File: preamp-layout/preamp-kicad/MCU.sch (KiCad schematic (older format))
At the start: 10 parts, among them J20 Conn_01x15_Female, J21 Conn_01x15_Female, J22 Conn_01x06_Female, J23 Conn_01x03_Female, J24 Conn_01x03_Female, J25 Conn_01x03_Female, J26 Conn_01x03_Male, J27 Conn_01x02_Male, J28 Conn_01x02_Male, U5 ESP32-DevKitC

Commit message: BOM Update
parts added to BOM, connector cleanup. Stopping point before renumbering refdes in a more intelligent way.
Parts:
- renumbered J20 to J27, J21 to J28, J22 to J29, J23 to J30, J24 to J31, J25 to J32, J26 to J33, J27 to J34, J28 to J35
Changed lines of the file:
@@
 $Descr A4 11693 8268
 encoding utf-8
-Sheet 7 13
+Sheet 6 13
 Title "Preamp MCU Board"
 Date "2020-02-25"
@@
 PWR, monitoring
 $Comp
-L Connector:Conn_01x02_Male J28
+L Connector:Conn_01x02_Male J35
 U 1 1 63AD6EFD
 P 8600 3750
-F 0 "J28" H 8572 3678 50  0000 R CNN
+F 0 "J35" H 8572 3678 50  0000 R CNN
 F 1 "Conn_01x02_Male" H 8572 3633 50  0001 R CNN
 F 2 "Connector_JST:JST_EH_B2B-EH-A_1x02_P2.50mm_Vertical" H 8600 3750 50  0001 C CNN
@@
 AR Path="/5E607732/6496C10E" Ref="J?"  Part="1"
 AR Path="/5E2D8DA2/6496C10E" Ref="J?"  Part="1"
-AR Path="/619FA14B/6496C10E" Ref="J23"  Part="1"
-F 0 "J23" H 7278 4180 50  0000 L CNN
+AR Path="/619FA14B/6496C10E" Ref="J30"  Part="1"
+F 0 "J30" H 7278 4180 50  0000 L CNN
 F 1 "Conn_01x03_Female" H 7278 4135 50  0001 L CNN
 F 2 "Connector_PinHeader_2.54mm:PinHeader_1x03_P2.54mm_Vertical" H 7250 4200 50  0001 C CNN
@@
 P 8350 4900
 AR Path="/5E2D8DA2/6496C114" Ref="J?"  Part="1"
-AR Path="/619FA14B/6496C114" Ref="J26"  Part="1"
-F 0 "J26" H 8322 4878 50  0000 R CNN
+AR Path="/619FA14B/6496C114" Ref="J33"  Part="1"
+F 0 "J33" H 8322 4878 50  0000 R CNN
 F 1 "Conn_01x03_Male" H 8322 4833 50  0001 R CNN
 F 2 "Connector_PinHeader_2.54mm:PinHeader_1x03_P2.54mm_Vertical" H 8350 4900 50  0001 C CNN
@@
 AR Path="/5E607732/6496FD14" Ref="J?"  Part="1"
 AR Path="/5E2D8DA2/6496FD14" Ref="J?"  Part="1"
-AR Path="/619FA14B/6496FD14" Ref="J24"  Part="1"
-F 0 "J24" H 7278 4630 50  0000 L CNN
+AR Path="/619FA14B/6496FD14" Ref="J31"  Part="1"
+F 0 "J31" H 7278 4630 50  0000 L CNN
 F 1 "Conn_01x03_Female" H 7278 4585 50  0001 L CNN
 F 2 "Connector_PinHeader_2.54mm:PinHeader_1x03_P2.54mm_Vertical" H 7250 4650 50  0001 C CNN
@@
 AR Path="/5E607732/64973E6E" Ref="J?"  Part="1"
 AR Path="/5E2D8DA2/64973E6E" Ref="J?"  Part="1"
-AR Path="/619FA14B/64973E6E" Ref="J25"  Part="1"
-F 0 "J25" H 7278 5080 50  0000 L CNN
+AR Path="/619FA14B/64973E6E" Ref="J32"  Part="1"
+F 0 "J32" H 7278 5080 50  0000 L CNN
 F 1 "Conn_01x03_Female" H 7278 5035 50  0001 L CNN
 F 2 "Connector_PinHeader_2.54mm:PinHeader_1x03_P2.54mm_Vertical" H 7250 5100 50  0001 C CNN
@@
 MISO
 $Comp
-L Connector:Conn_01x06_Female J22
+L Connector:Conn_01x06_Female J29
 U 1 1 64977856
 P 7250 3350
-F 0 "J22" H 7278 3280 50  0000 L CNN
+F 0 "J29" H 7278 3280 50  0000 L CNN
 F 1 "Conn_01x06_Female" H 7278 3235 50  0001 L CNN
 F 2 "Connector_PinHeader_2.54mm:PinHeader_1x06_P2.54mm_Vertical" H 7250 3350 50  0001 C CNN
@@
 CS_IO
 $Comp
-L Connector:Conn_01x15_Female J21
+L Connector:Conn_01x15_Female J28
 U 1 1 649C22F5
 P 5200 3850
-F 0 "J21" H 5092 4643 50  0000 C CNN
+F 0 "J28" H 5092 4643 50  0000 C CNN
 F 1 "Conn_01x15_Female" H 5092 4644 50  0001 C CNN
 F 2 "Connector_PinHeader_2.54mm:PinHeader_1x15_P2.54mm_Vertical" H 5200 3850 50  0001 C CNN
@@
 $EndComp
 $Comp
-L Connector:Conn_01x15_Female J20
+L Connector:Conn_01x15_Female J27
 U 1 1 649C438C
 P 3800 3850
-F 0 "J20" H 3828 3830 50  0000 L CNN
+F 0 "J27" H 3828 3830 50  0000 L CNN
 F 1 "Conn_01x15_Female" H 3828 3785 50  0001 L CNN
 F 2 "Connector_PinHeader_2.54mm:PinHeader_1x15_P2.54mm_Vertical" H 3800 3850 50  0001 C CNN
@@
 P 3350 4750
 AR Path="/5E26F6FE/64EF3AEF" Ref="#PWR?"  Part="1"
-AR Path="/619FA14B/64EF3AEF" Ref="#PWR024"  Part="1"
-F 0 "#PWR024" H 3350 4500 50  0001 C CNN
+AR Path="/619FA14B/64EF3AEF" Ref="#PWR031"  Part="1"
+F 0 "#PWR031" H 3350 4500 50  0001 C CNN
 F 1 "GND" H 3355 4577 50  0000 C CNN
 F 2 "" H 3350 4750 50  0001 C CNN
@@
 P 8400 3400
 AR Path="/5E26F6FE/64EF440C" Ref="#PWR?"  Part="1"
-AR Path="/619FA14B/64EF440C" Ref="#PWR025"  Part="1"
-F 0 "#PWR025" H 8400 3150 50  0001 C CNN
+AR Path="/619FA14B/64EF440C" Ref="#PWR033"  Part="1"
+F 0 "#PWR033" H 8400 3150 50  0001 C CNN
 F 1 "GND" H 8405 3227 50  0000 C CNN
 F 2 "" H 8400 3400 50  0001 C CNN
@@
 P 8400 3950
 AR Path="/5E26F6FE/64EF4C33" Ref="#PWR?"  Part="1"
-AR Path="/619FA14B/64EF4C33" Ref="#PWR026"  Part="1"
-F 0 "#PWR026" H 8400 3700 50  0001 C CNN
+AR Path="/619FA14B/64EF4C33" Ref="#PWR034"  Part="1"
+F 0 "#PWR034" H 8400 3700 50  0001 C CNN
 F 1 "GND" H 8405 3777 50  0000 C CNN
 F 2 "" H 8400 3950 50  0001 C CNN
@@
 NoConn ~ 7050 3650
 $Comp
-L Connector:Conn_01x02_Male J27
+L Connector:Conn_01x02_Male J34
 U 1 1 5E6537E3
 P 8600 3200
-F 0 "J27" H 8572 3128 50  0000 R CNN
+F 0 "J34" H 8572 3128 50  0000 R CNN
 F 1 "Conn_01x02_Male" H 8572 3083 50  0001 R CNN
 F 2 "Connector_JST:JST_EH_B2B-EH-A_1x02_P2.50mm_Vertical" H 8600 3200 50  0001 C CNN
@@
 P 8050 5100
 AR Path="/5E26F6FE/5EA8A311" Ref="#PWR?"  Part="1"
-AR Path="/619FA14B/5EA8A311" Ref="#PWR021"  Part="1"
-F 0 "#PWR021" H 8050 4850 50  0001 C CNN
+AR Path="/619FA14B/5EA8A311" Ref="#PWR032"  Part="1"
+F 0 "#PWR032" H 8050 4850 50  0001 C CNN
 F 1 "GND" H 8055 4927 50  0000 C CNN
 F 2 "" H 8050 5100 50  0001 C CNN

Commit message: Schematic Updates
Updated pin connections for DAC, footprint updates, MCU connections.
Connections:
- wire segments 21 -> 5
- no-connect marks 51 -> 46
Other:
- moved on the sheet: J33, J35
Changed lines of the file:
@@
 Comment4 "Author: Jordon Gerber"
 $EndDescr
-Text HLabel 3550 2200 0    50   Input ~ 0
+Text HLabel 5400 3250 2    50   Input ~ 0
 MISO
-Text HLabel 5700 3150 2    50   Output ~ 0
+Text HLabel 5400 3150 2    50   Output ~ 0
 MOSI
-Text HLabel 5700 3750 2    50   Output ~ 0
+Text HLabel 5400 3750 2    50   Output ~ 0
 CLK
-Text HLabel 5700 3850 2    50   Output ~ 0
+Text HLabel 5400 3850 2    50   Output ~ 0
 CS_IO
 Wire Wire Line
-	8400 3850 8400 3950
-Wire Wire Line
-	8300 3750 8400 3750
-Text GLabel 8300 3750 0    50   UnSpc ~ 0
+	8400 3950 8400 4050
+Text GLabel 8400 3850 0    50   UnSpc ~ 0
 +5V
 Wire Wire Line
 	8400 3300 8400 3400
-Wire Wire Line
-	8300 3200 8400 3200
-Text GLabel 8300 3200 0    50   UnSpc ~ 0
+Text GLabel 8400 3200 0    50   UnSpc ~ 0
 +5V
 Text Notes 8150 2750 0    50   ~ 0
@@
 L Connector:Conn_01x02_Male J35
 U 1 1 63AD6EFD
-P 8600 3750
-F 0 "J35" H 8572 3678 50  0000 R CNN
-F 1 "Conn_01x02_Male" H 8572 3633 50  0001 R CNN
-F 2 "Connector_JST:JST_EH_B2B-EH-A_1x02_P2.50mm_Vertical" H 8600 3750 50  0001 C CNN
-F 3 "~" H 8600 3750 50  0001 C CNN
-	1    8600 3750
-	-1   0    0    -1
-$EndComp
-Text HLabel 3300 3750 0    50   Input ~ 0
+P 8600 3850
+F 0 "J35" H 8572 3778 50  0000 R CNN
+F 1 "Conn_01x02_Male" H 8572 3733 50  0001 R CNN
+F 2 "Connector_JST:JST_EH_B2B-EH-A_1x02_P2.50mm_Vertical" H 8600 3850 50  0001 C CNN
+F 3 "~" H 8600 3850 50  0001 C CNN
+	1    8600 3850
+	-1   0    0    -1
+$EndComp
+Text HLabel 3600 3750 0    50   Input ~ 0
 SEL_CLK
-Text HLabel 3300 3950 0    50   Input ~ 0
+Text HLabel 3600 3950 0    50   Input ~ 0
 SEL_SW
-Text HLabel 3300 4050 0    50   Input ~ 0
+Text HLabel 3600 4050 0    50   Input ~ 0
 VOL_CLK
-Text HLabel 3300 4150 0    50   Input ~ 0
+Text HLabel 3600 4150 0    50   Input ~ 0
 VOL_DT
-Text HLabel 3300 4350 0    50   Input ~ 0
+Text HLabel 3600 4350 0    50   Input ~ 0
 VOL_SW
-Text HLabel 3550 2400 0    50   Output ~ 0
+Text HLabel 5400 4150 2    50   Output ~ 0
 CS_FP
-Text HLabel 3550 2500 0    50   Output ~ 0
+Text HLabel 5400 4050 2    50   Output ~ 0
 CS_VOL_HP
 Text HLabel 8050 4900 0    50   Output ~ 0
 LED_DT
-Text HLabel 3550 2600 0    50   Output ~ 0
+Text HLabel 5400 3950 2    50   Output ~ 0
 CS_VOL_MAIN
-Text GLabel 3550 4700 3    50   UnSpc ~ 0
+Text GLabel 3600 4550 0    50   UnSpc ~ 0
 +5V
 Wire Wire Line
@@
 	1    0    0    -1
 $EndComp
-Text HLabel 3300 3850 0    50   Input ~ 0
+Text HLabel 3600 3850 0    50   Input ~ 0
 SEL_DT
 Wire Wire Line
-	3550 4550 3600 4550
-Wire Wire Line
-	3550 4550 3550 4700
-Wire Wire Line
 	3350 4450 3600 4450
-Wire Wire Line
-	3300 3750 3600 3750
-Wire Wire Line
-	3300 3850 3600 3850
-Wire Wire Line
-	3300 3950 3600 3950
-Wire Wire Line
-	3300 4050 3600 4050
-Wire Wire Line
-	3300 4150 3600 4150
-Wire Wire Line
-	3300 4350 3600 4350
-Wire Wire Line
-	5400 3150 5700 3150
-Wire Wire Line
-	5400 3750 5700 3750
-Wire Wire Line
-	5400 3850 5700 3850
 $Comp
 L Connector:Conn_01x03_Female J?
@@
 L Connector:Conn_01x03_Male J?
 U 1 1 6496C114
-P 8350 4900
+P 8250 4900
 AR Path="/5E2D8DA2/6496C114" Ref="J?"  Part="1"
 AR Path="/619FA14B/6496C114" Ref="J33"  Part="1"
-F 0 "J33" H 8322 4878 50  0000 R CNN
-F 1 "Conn_01x03_Male" H 8322 4833 50  0001 R CNN
-F 2 "Connector_PinHeader_2.54mm:PinHeader_1x03_P2.54mm_Vertical" H 8350 4900 50  0001 C CNN
-F 3 "~" H 8350 4900 50  0001 C CNN
-	1    8350 4900
+F 0 "J33" H 8222 4878 50  0000 R CNN
+F 1 "Conn_01x03_Male" H 8222 4833 50  0001 R CNN
+F 2 "Connector_PinHeader_2.54mm:PinHeader_1x03_P2.54mm_Vertical" H 8250 4900 50  0001 C CNN
+F 3 "~" H 8250 4900 50  0001 C CNN
+	1    8250 4900
 	-1   0    0    -1
 $EndComp
@@
 L power:GND #PWR?
 U 1 1 64EF4C33
-P 8400 3950
+P 8400 4050
 AR Path="/5E26F6FE/64EF4C33" Ref="#PWR?"  Part="1"
 AR Path="/619FA14B/64EF4C33" Ref="#PWR034"  Part="1"
-F 0 "#PWR034" H 8400 3700 50  0001 C CNN
-F 1 "GND" H 8405 3777 50  0000 C CNN
-F 2 "" H 8400 3950 50  0001 C CNN
-F 3 "" H 8400 3950 50  0001 C CNN
-	1    8400 3950
+F 0 "#PWR034" H 8400 3800 50  0001 C CNN
+F 1 "GND" H 8405 3877 50  0000 C CNN
+F 2 "" H 8400 4050 50  0001 C CNN
+F 3 "" H 8400 4050 50  0001 C CNN
+	1    8400 4050
 	1    0    0    -1
 $EndComp
@@
 NoConn ~ 4950 3350
 NoConn ~ 4950 3450
-NoConn ~ 5400 3250
 NoConn ~ 5400 3350
 NoConn ~ 5400 3450
 NoConn ~ 5400 3550
 NoConn ~ 5400 3650
-NoConn ~ 5400 3950
-NoConn ~ 5400 4050
-NoConn ~ 5400 4150
 NoConn ~ 5400 4250
 NoConn ~ 5400 4350
@@
 NoConn ~ 3600 3250
 NoConn ~ 3600 3350
-NoConn ~ 3600 3450
 NoConn ~ 3600 3550
 NoConn ~ 3600 3650
@@
 Text GLabel 8050 4800 0    50   UnSpc ~ 0
 +5V
-Wire Wire Line
-	8050 4800 8150 4800
-Wire Wire Line
-	8050 4900 8150 4900
-Wire Wire Line
-	8050 5000 8150 5000
+Text HLabel 3600 3450 0    50   Output ~ 0
+LED_DT
 $EndSCHEMATC

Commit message: Footprint updates
Footprint creation of relay, ESP32
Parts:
- removed J27, J28: Conn_01x15_Female, Connector_PinHeader_2.54mm:PinHeader_1x15_P2.54mm_Vertical, symbol Connector:Conn_01x15_Female
- U5: footprint (none) -> preamp:ESP32_MELIFE_DEVKIT
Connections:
- wire segments 5 -> 34
- no-connect marks 46 -> 16
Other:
- moved on the sheet: U5
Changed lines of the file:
@@
 Comment4 "Author: Jordon Gerber"
 $EndDescr
-Text HLabel 5400 3250 2    50   Input ~ 0
-MISO
-Text HLabel 5400 3150 2    50   Output ~ 0
-MOSI
-Text HLabel 5400 3750 2    50   Output ~ 0
-CLK
-Text HLabel 5400 3850 2    50   Output ~ 0
-CS_IO
 Wire Wire Line
 	8400 3950 8400 4050
@@
 	-1   0    0    -1
 $EndComp
-Text HLabel 3600 3750 0    50   Input ~ 0
+Text HLabel 4000 3550 0    50   Input ~ 0
 SEL_CLK
-Text HLabel 3600 3950 0    50   Input ~ 0
+Text HLabel 4000 3750 0    50   Input ~ 0
 SEL_SW
-Text HLabel 3600 4050 0    50   Input ~ 0
+Text HLabel 4000 3850 0    50   Input ~ 0
 VOL_CLK
-Text HLabel 3600 4150 0    50   Input ~ 0
+Text HLabel 4000 3950 0    50   Input ~ 0
 VOL_DT
-Text HLabel 3600 4350 0    50   Input ~ 0
+Text HLabel 4000 4150 0    50   Input ~ 0
 VOL_SW
-Text HLabel 5400 4150 2    50   Output ~ 0
-CS_FP
-Text HLabel 5400 4050 2    50   Output ~ 0
-CS_VOL_HP
 Text HLabel 8050 4900 0    50   Output ~ 0
 LED_DT
-Text HLabel 5400 3950 2    50   Output ~ 0
-CS_VOL_MAIN
-Text GLabel 3600 4550 0    50   UnSpc ~ 0
+Text GLabel 4000 4350 0    50   UnSpc ~ 0
 +5V
 Wire Wire Line
-	3350 4750 3350 4450
+	3750 4550 3750 4250
 $Comp
 L preamp:ESP32-DevKitC U5
 U 1 1 64954378
-P 4500 3850
-F 0 "U5" H 4500 4815 50  0000 C CNN
-F 1 "ESP32-DevKitC" H 4500 4724 50  0000 C CNN
-F 2 "" H 4500 4850 50  0001 C CNN
-F 3 "" H 4500 4850 50  0001 C CNN
-	1    4500 3850
-	1    0    0    -1
-$EndComp
-Text HLabel 3600 3850 0    50   Input ~ 0
+P 4550 3650
+F 0 "U5" H 4550 4615 50  0000 C CNN
+F 1 "ESP32-DevKitC" H 4550 4524 50  0000 C CNN
+F 2 "preamp:ESP32_MELIFE_DEVKIT" H 4550 4650 50  0001 C CNN
+F 3 "" H 4550 4650 50  0001 C CNN
+	1    4550 3650
+	1    0    0    -1
+$EndComp
+Text HLabel 4000 3650 0    50   Input ~ 0
 SEL_DT
-Wire Wire Line
-	3350 4450 3600 4450
 $Comp
 L Connector:Conn_01x03_Female J?
@@
 CS_IO
 $Comp
-L Connector:Conn_01x15_Female J28
-U 1 1 649C22F5
-P 5200 3850
-F 0 "J28" H 5092 4643 50  0000 C CNN
-F 1 "Conn_01x15_Female" H 5092 4644 50  0001 C CNN
-F 2 "Connector_PinHeader_2.54mm:PinHeader_1x15_P2.54mm_Vertical" H 5200 3850 50  0001 C CNN
-F 3 "~" H 5200 3850 50  0001 C CNN
-	1    5200 3850
-	-1   0    0    -1
-$EndComp
-$Comp
-L Connector:Conn_01x15_Female J27
-U 1 1 649C438C
-P 3800 3850
-F 0 "J27" H 3828 3830 50  0000 L CNN
-F 1 "Conn_01x15_Female" H 3828 3785 50  0001 L CNN
-F 2 "Connector_PinHeader_2.54mm:PinHeader_1x15_P2.54mm_Vertical" H 3800 3850 50  0001 C CNN
-F 3 "~" H 3800 3850 50  0001 C CNN
-	1    3800 3850
-	1    0    0    -1
-$EndComp
-$Comp
 L power:GND #PWR?
 U 1 1 64EF3AEF
-P 3350 4750
+P 3750 4550
 AR Path="/5E26F6FE/64EF3AEF" Ref="#PWR?"  Part="1"
 AR Path="/619FA14B/64EF3AEF" Ref="#PWR031"  Part="1"
-F 0 "#PWR031" H 3350 4500 50  0001 C CNN
-F 1 "GND" H 3355 4577 50  0000 C CNN
-F 2 "" H 3350 4750 50  0001 C CNN
-F 3 "" H 3350 4750 50  0001 C CNN
-	1    3350 4750
+F 0 "#PWR031" H 3750 4300 50  0001 C CNN
+F 1 "GND" H 3755 4377 50  0000 C CNN
+F 2 "" H 3750 4550 50  0001 C CNN
+F 3 "" H 3750 4550 50  0001 C CNN
+	1    3750 4550
 	1    0    0    -1
 $EndComp
@@
 	1    0    0    -1
 $EndComp
-NoConn ~ 4950 4550
-NoConn ~ 4950 4450
-NoConn ~ 4950 4350
-NoConn ~ 4950 4250
-NoConn ~ 4950 4150
-NoConn ~ 4950 4050
-NoConn ~ 4950 3950
-NoConn ~ 4950 3850
-NoConn ~ 4950 3750
-NoConn ~ 4950 3650
-NoConn ~ 4950 3550
-NoConn ~ 4950 3150
-NoConn ~ 4950 3250
-NoConn ~ 4950 3350
-NoConn ~ 4950 3450
-NoConn ~ 5400 3350
-NoConn ~ 5400 3450
-NoConn ~ 5400 3550
-NoConn ~ 5400 3650
-NoConn ~ 5400 4250
-NoConn ~ 5400 4350
-NoConn ~ 5400 4450
-NoConn ~ 5400 4550
-NoConn ~ 4050 4550
-NoConn ~ 4050 4450
-NoConn ~ 4050 4350
-NoConn ~ 4050 4250
-NoConn ~ 4050 4150
-NoConn ~ 4050 4050
-NoConn ~ 4050 3950
-NoConn ~ 4050 3850
-NoConn ~ 4050 3750
-NoConn ~ 4050 3650
-NoConn ~ 4050 3550
-NoConn ~ 4050 3450
-NoConn ~ 4050 3350
-NoConn ~ 4050 3250
-NoConn ~ 4050 3150
-NoConn ~ 3600 3150
-NoConn ~ 3600 3250
-NoConn ~ 3600 3350
-NoConn ~ 3600 3550
-NoConn ~ 3600 3650
-NoConn ~ 3600 4250
+NoConn ~ 4000 2950
+NoConn ~ 4000 3050
+NoConn ~ 4000 3150
+NoConn ~ 4000 3350
+NoConn ~ 4000 3450
+NoConn ~ 4000 4050
 NoConn ~ 7050 3550
 NoConn ~ 7050 3650
@@
 Text GLabel 8050 4800 0    50   UnSpc ~ 0
 +5V
-Text HLabel 3600 3450 0    50   Output ~ 0
+Text HLabel 4000 3250 0    50   Output ~ 0
 LED_DT
+NoConn ~ 5100 4350
+NoConn ~ 5100 4250
+NoConn ~ 5100 4150
+NoConn ~ 5100 4050
+NoConn ~ 5100 3450
+NoConn ~ 5100 3350
+NoConn ~ 5100 3250
+NoConn ~ 5100 3150
+Text HLabel 5100 3750 2    50   Output ~ 0
+CS_VOL_MAIN
+Text HLabel 5100 3850 2    50   Output ~ 0
+CS_VOL_HP
+Text HLabel 5100 3950 2    50   Output ~ 0
+CS_FP
+Text HLabel 5100 3650 2    50   Output ~ 0
+CS_IO
+Text HLabel 5100 3550 2    50   Output ~ 0
+CLK
+Text HLabel 5100 2950 2    50   Output ~ 0
+MOSI
+Text HLabel 5100 3050 2    50   Input ~ 0
+MISO
+Wire Wire Line
+	5000 3050 5100 3050
+Wire Wire Line
+	5000 2950 5100 2950
+Wire Wire Line
+	5000 3250 5100 3250
+Wire Wire Line
+	5000 3150 5100 3150
+Wire Wire Line
+	5000 3450 5100 3450
+Wire Wire Line
+	5000 3350 5100 3350
+Wire Wire Line
+	5000 3650 5100 3650
+Wire Wire Line
+	5000 3550 5100 3550
+Wire Wire Line
+	5000 3850 5100 3850
+Wire Wire Line
+	5000 3750 5100 3750
+Wire Wire Line
+	5000 4050 5100 4050
+Wire Wire Line
+	5000 3950 5100 3950
+Wire Wire Line
+	5000 4250 5100 4250
+Wire Wire Line
+	5000 4150 5100 4150
+Wire Wire Line
+	5000 4350 5100 4350
+Wire Wire Line
+	4000 3050 4100 3050
+Wire Wire Line
+	4000 2950 4100 2950
+Wire Wire Line
+	4000 3250 4100 3250
+Wire Wire Line
+	4000 3150 4100 3150
+Wire Wire Line
+	4000 3450 4100 3450
+Wire Wire Line
+	4000 3350 4100 3350
+Wire Wire Line
+	4000 3650 4100 3650
+Wire Wire Line
+	4000 3550 4100 3550
+Wire Wire Line
+	4000 3850 4100 3850
+Wire Wire Line
+	4000 3750 4100 3750
+Wire Wire Line
+	4000 4050 4100 4050
+Wire Wire Line
+	4000 3950 4100 3950
+Wire Wire Line
+	4000 4150 4100 4150
+Wire Wire Line
+	4000 4350 4100 4350
+Wire Wire Line
+	3750 4250 4100 4250
 $EndSCHEMATC

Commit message: Conn / Pin Updates
Updated cable headers, pin names, MCU conn layout. MCP4902 changeout for custom symbol.
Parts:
- removed J29: Conn_01x06_Female, Connector_PinHeader_2.54mm:PinHeader_1x06_P2.54mm_Vertical, symbol Connector:Conn_01x06_Female
- removed J30, J31, J32: Conn_01x03_Female, Connector_PinHeader_2.54mm:PinHeader_1x03_P2.54mm_Vertical, symbol Connector:Conn_01x03_Female
- added J27, J32: Conn_01x04_Female, symbol Connector:Conn_01x04_Female
- added J29, J30, J31: Conn_01x05_Female, symbol Connector:Conn_01x05_Female
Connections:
- net labels added: SW_INT, ~CS_FP, ~CS_IO, ~CS_VOL_HP, ~CS_VOL_MAIN
- net labels removed: CS_FP, CS_IO, CS_VOL_HP, CS_VOL_MAIN
- wire segments 34 -> 63
- no-connect marks 16 -> 12
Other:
- note removed: "PWR, monitoring"
- moved on the sheet: J33, J34, J35, U5

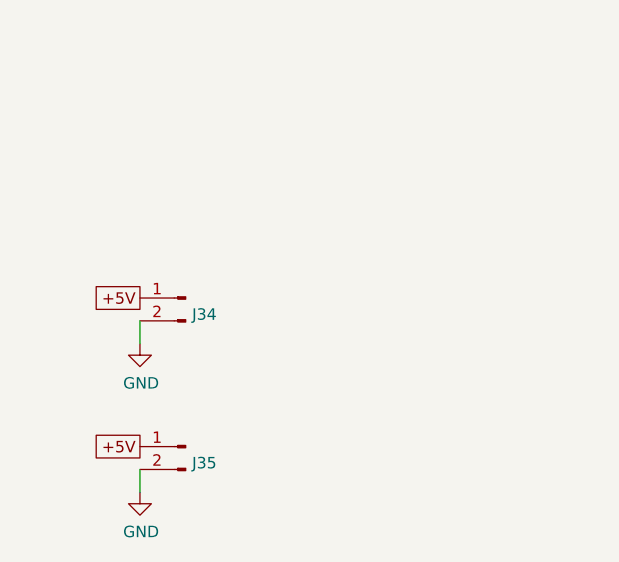
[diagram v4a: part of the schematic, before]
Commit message: Power Supply Update
Grounding made more clear, tied to chassis on AC board. Pins renamed. Aligned with AC wall power convention. General cleanup.
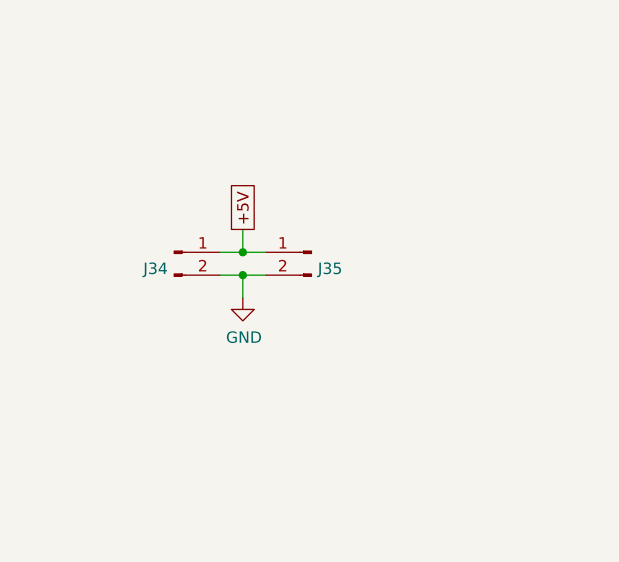
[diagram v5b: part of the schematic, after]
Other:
- moved on the sheet: J34, J35
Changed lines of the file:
@@
 $EndDescr
 Wire Wire Line
-	3600 6600 3600 6700
-Text GLabel 3600 6500 0    50   UnSpc ~ 0
-+5V
-Wire Wire Line
-	3600 5950 3600 6050
-Text GLabel 3600 5850 0    50   UnSpc ~ 0
+	4050 5750 4050 5850
+Text GLabel 4050 5550 1    50   UnSpc ~ 0
 +5V
 $Comp
 L Connector:Conn_01x02_Male J35
 U 1 1 63AD6EFD
-P 3800 6500
-F 0 "J35" H 3772 6428 50  0000 R CNN
-F 1 "Conn_01x02_Male" H 3772 6383 50  0001 R CNN
-F 2 "Connector_JST:JST_EH_B2B-EH-A_1x02_P2.50mm_Vertical" H 3800 6500 50  0001 C CNN
-F 3 "~" H 3800 6500 50  0001 C CNN
-	1    3800 6500
+P 4350 5650
+F 0 "J35" H 4322 5578 50  0000 R CNN
+F 1 "Conn_01x02_Male" H 4322 5533 50  0001 R CNN
+F 2 "Connector_JST:JST_EH_B2B-EH-A_1x02_P2.50mm_Vertical" H 4350 5650 50  0001 C CNN
+F 3 "~" H 4350 5650 50  0001 C CNN
+	1    4350 5650
 	-1   0    0    -1
 $EndComp
@@
 $Comp
 L power:GND #PWR?
-U 1 1 64EF440C
-P 3600 6050
-AR Path="/5E26F6FE/64EF440C" Ref="#PWR?"  Part="1"
-AR Path="/619FA14B/64EF440C" Ref="#PWR033"  Part="1"
-F 0 "#PWR033" H 3600 5800 50  0001 C CNN
-F 1 "GND" H 3605 5877 50  0000 C CNN
-F 2 "" H 3600 6050 50  0001 C CNN
-F 3 "" H 3600 6050 50  0001 C CNN
-	1    3600 6050
-	1    0    0    -1
-$EndComp
-$Comp
-L power:GND #PWR?
 U 1 1 64EF4C33
-P 3600 6700
+P 4050 5850
 AR Path="/5E26F6FE/64EF4C33" Ref="#PWR?"  Part="1"
 AR Path="/619FA14B/64EF4C33" Ref="#PWR034"  Part="1"
-F 0 "#PWR034" H 3600 6450 50  0001 C CNN
-F 1 "GND" H 3605 6527 50  0000 C CNN
-F 2 "" H 3600 6700 50  0001 C CNN
-F 3 "" H 3600 6700 50  0001 C CNN
-	1    3600 6700
+F 0 "#PWR034" H 4050 5600 50  0001 C CNN
+F 1 "GND" H 4055 5677 50  0000 C CNN
+F 2 "" H 4050 5850 50  0001 C CNN
+F 3 "" H 4050 5850 50  0001 C CNN
+	1    4050 5850
 	1    0    0    -1
 $EndComp
@@
 L Connector:Conn_01x02_Male J34
 U 1 1 5E6537E3
-P 3800 5850
-F 0 "J34" H 3772 5778 50  0000 R CNN
-F 1 "Conn_01x02_Male" H 3772 5733 50  0001 R CNN
-F 2 "Connector_JST:JST_EH_B2B-EH-A_1x02_P2.50mm_Vertical" H 3800 5850 50  0001 C CNN
-F 3 "~" H 3800 5850 50  0001 C CNN
-	1    3800 5850
-	-1   0    0    -1
+P 3750 5650
+F 0 "J34" H 3722 5578 50  0000 R CNN
+F 1 "Conn_01x02_Male" H 3722 5533 50  0001 R CNN
+F 2 "Connector_JST:JST_EH_B2B-EH-A_1x02_P2.50mm_Vertical" H 3750 5650 50  0001 C CNN
+F 3 "~" H 3750 5650 50  0001 C CNN
+	1    3750 5650
+	1    0    0    -1
 $EndComp
 Wire Wire Line
@@
 Text HLabel 3500 2700 0    50   Input ~ 0
 SW_INT
+Wire Wire Line
+	3950 5650 4050 5650
+Wire Wire Line
+	3950 5750 4050 5750
+Connection ~ 4050 5750
+Wire Wire Line
+	4050 5750 4150 5750
+Wire Wire Line
+	4050 5650 4050 5550
+Connection ~ 4050 5650
+Wire Wire Line
+	4050 5650 4150 5650
 $EndSCHEMATC
